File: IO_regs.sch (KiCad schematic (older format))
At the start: 77 parts, among them U17 74HC04, U4 74HC04, U42 74HC245, U43 74HC04, U44 74HC04, U45 74LS373, U46 74HC04, U47 74HC04, U48 74HC04, U49 74HC04, U50 74HC04, U51 74HC04, U52 74HC04, U6 74HC04

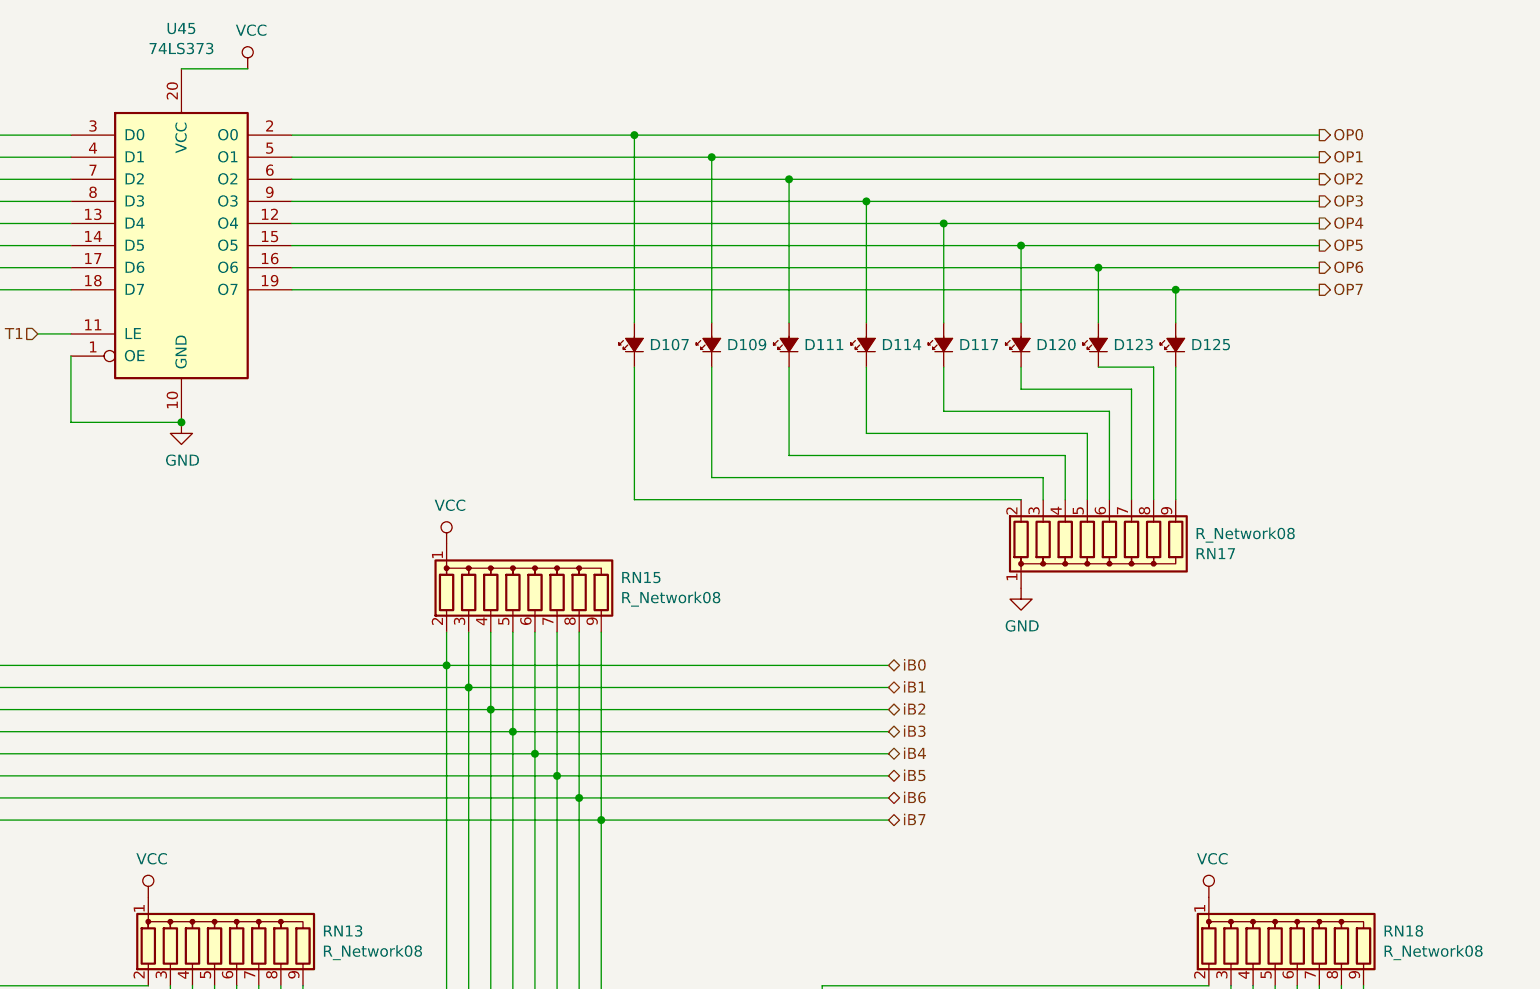
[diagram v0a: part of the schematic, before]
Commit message: start routing the OPcode register, we have a piece of the iBn bus
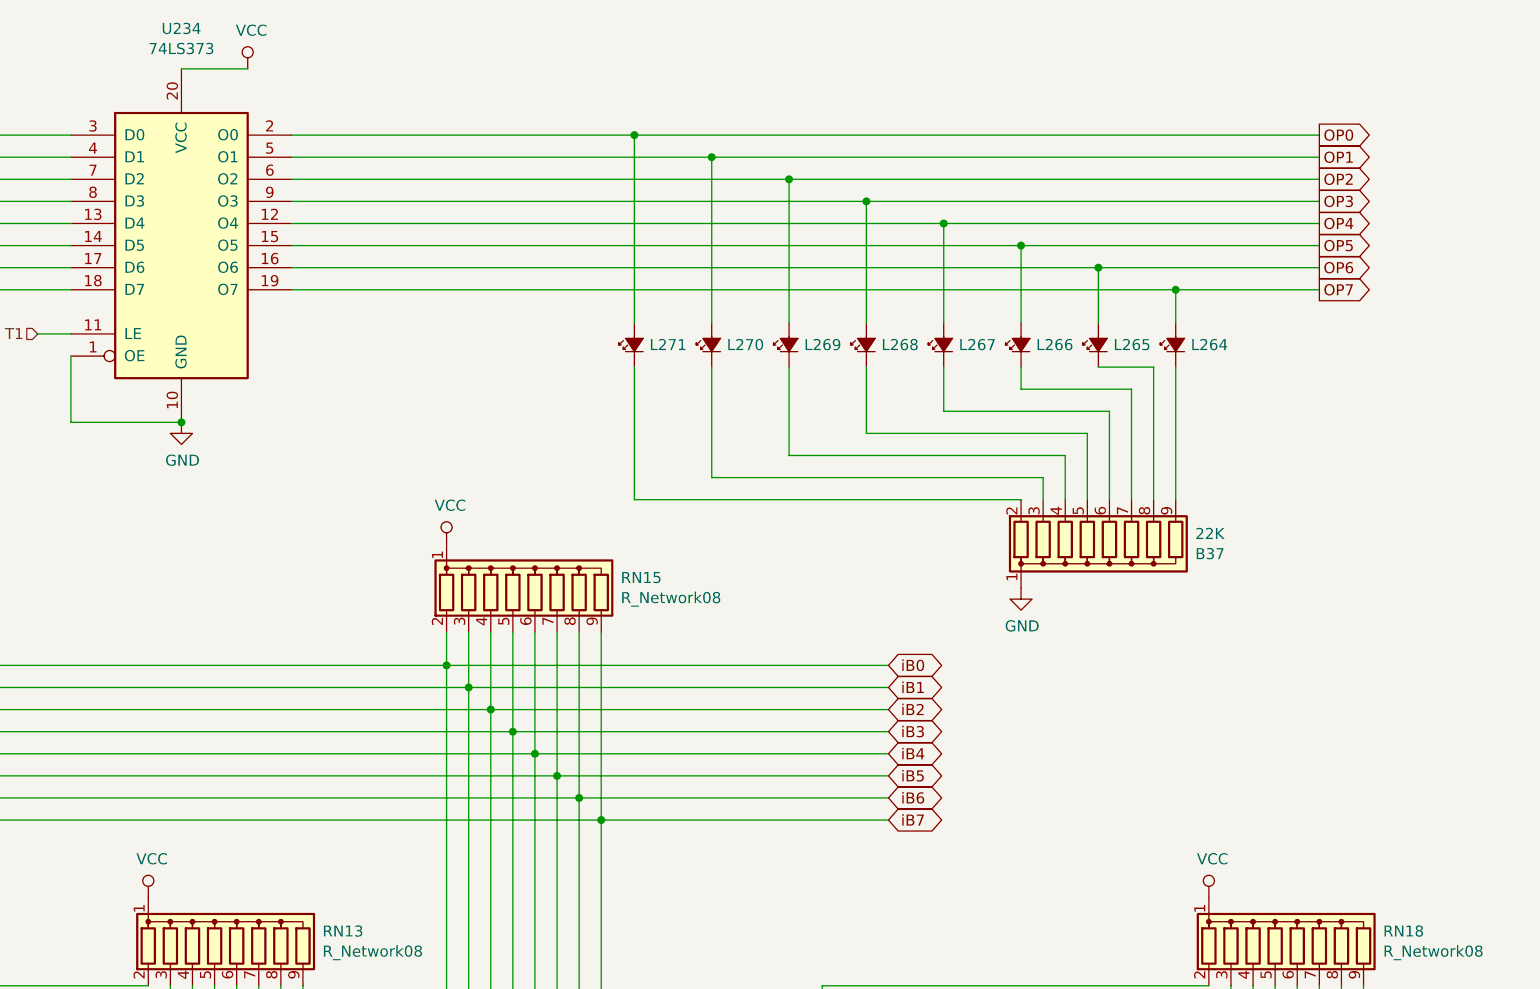
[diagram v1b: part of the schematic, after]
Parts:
- B37: renamed from RN17; value R_Network08 -> 22K
- renumbered D125 to L264, D123 to L265, D120 to L266, D117 to L267, D114 to L268, D111 to L269, D109 to L270, D107 to L271, U45 to U234
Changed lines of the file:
@@
 Wire Wire Line
 	6750 3800 6750 4650
-Text HLabel 8050 3950 2    50   BiDi ~ 0
-iB0
-Text HLabel 8050 4050 2    50   BiDi ~ 0
-iB1
-Text HLabel 8050 4150 2    50   BiDi ~ 0
-iB2
-Text HLabel 8050 4250 2    50   BiDi ~ 0
-iB3
-Text HLabel 8050 4350 2    50   BiDi ~ 0
-iB4
-Text HLabel 8050 4550 2    50   BiDi ~ 0
-iB6
-Text HLabel 8050 4650 2    50   BiDi ~ 0
-iB7
-$Comp
-L 74xx:74LS373 U45
+$Comp
+L 74xx:74LS373 U234
 U 1 1 5E589EDB
 P 4850 2050
-F 0 "U45" H 4850 3031 50  0000 C CNN
+F 0 "U234" H 4850 3031 50  0000 C CNN
 F 1 "74LS373" H 4850 2940 50  0000 C CNN
 F 2 "Package_DIP:DIP-20_W7.62mm" H 4850 2050 50  0001 C CNN
@@
 	3250 3950 6050 3950
 $Comp
-L Device:R_Network08 RN17
+L Device:R_Network08 B37
 U 1 1 5E61675D
 P 9050 3400
-F 0 "RN17" H 9438 3446 50  0000 L CNN
-F 1 "R_Network08" H 9438 3355 50  0000 L CNN
+F 0 "B37" H 9438 3446 50  0000 L CNN
+F 1 "22K" H 9438 3355 50  0000 L CNN
 F 2 "Resistor_THT:R_Array_SIP9" V 9525 3400 50  0001 C CNN
 F 3 "http://www.vishay.com/docs/31509/csc.pdf" H 9050 3400 50  0001 C CNN
@@
 $EndComp
 $Comp
-L Device:LED_Small_ALT D107
+L Device:LED_Small_ALT L271
 U 1 1 5E616763
 P 6900 2500
-F 0 "D107" V 6900 2432 50  0000 R CNN
+F 0 "L271" V 6900 2432 50  0000 R CNN
 F 1 "LED_Small_ALT" V 6855 2432 50  0001 R CNN
 F 2 "LED_THT:LED_D3.0mm" V 6900 2500 50  0001 C CNN
@@
 $EndComp
 $Comp
-L Device:LED_Small_ALT D109
+L Device:LED_Small_ALT L270
 U 1 1 5E616769
 P 7250 2500
-F 0 "D109" V 7250 2432 50  0000 R CNN
+F 0 "L270" V 7250 2432 50  0000 R CNN
 F 1 "LED_Small_ALT" V 7205 2432 50  0001 R CNN
 F 2 "LED_THT:LED_D3.0mm" V 7250 2500 50  0001 C CNN
@@
 $EndComp
 $Comp
-L Device:LED_Small_ALT D111
+L Device:LED_Small_ALT L269
 U 1 1 5E61676F
 P 7600 2500
-F 0 "D111" V 7600 2432 50  0000 R CNN
+F 0 "L269" V 7600 2432 50  0000 R CNN
 F 1 "LED_Small_ALT" V 7555 2432 50  0001 R CNN
 F 2 "LED_THT:LED_D3.0mm" V 7600 2500 50  0001 C CNN
@@
 $EndComp
 $Comp
-L Device:LED_Small_ALT D114
+L Device:LED_Small_ALT L268
 U 1 1 5E616775
 P 7950 2500
-F 0 "D114" V 7950 2432 50  0000 R CNN
+F 0 "L268" V 7950 2432 50  0000 R CNN
 F 1 "LED_Small_ALT" V 7905 2432 50  0001 R CNN
 F 2 "LED_THT:LED_D3.0mm" V 7950 2500 50  0001 C CNN
@@
 $EndComp
 $Comp
-L Device:LED_Small_ALT D117
+L Device:LED_Small_ALT L267
 U 1 1 5E61677B
 P 8300 2500
-F 0 "D117" V 8300 2432 50  0000 R CNN
+F 0 "L267" V 8300 2432 50  0000 R CNN
 F 1 "LED_Small_ALT" V 8255 2432 50  0001 R CNN
 F 2 "LED_THT:LED_D3.0mm" V 8300 2500 50  0001 C CNN
@@
 $EndComp
 $Comp
-L Device:LED_Small_ALT D120
+L Device:LED_Small_ALT L266
 U 1 1 5E616781
 P 8650 2500
-F 0 "D120" V 8650 2432 50  0000 R CNN
+F 0 "L266" V 8650 2432 50  0000 R CNN
 F 1 "LED_Small_ALT" V 8605 2432 50  0001 R CNN
 F 2 "LED_THT:LED_D3.0mm" V 8650 2500 50  0001 C CNN
@@
 $EndComp
 $Comp
-L Device:LED_Small_ALT D123
+L Device:LED_Small_ALT L265
 U 1 1 5E616787
 P 9000 2500
-F 0 "D123" V 9000 2432 50  0000 R CNN
+F 0 "L265" V 9000 2432 50  0000 R CNN
 F 1 "LED_Small_ALT" V 8955 2432 50  0001 R CNN
 F 2 "LED_THT:LED_D3.0mm" V 9000 2500 50  0001 C CNN
@@
 $EndComp
 $Comp
-L Device:LED_Small_ALT D125
+L Device:LED_Small_ALT L264
 U 1 1 5E61678D
 P 9350 2500
-F 0 "D125" V 9350 2432 50  0000 R CNN
+F 0 "L264" V 9350 2432 50  0000 R CNN
 F 1 "LED_Small_ALT" V 9305 2432 50  0001 R CNN
 F 2 "LED_THT:LED_D3.0mm" V 9350 2500 50  0001 C CNN
@@
 Wire Wire Line
 	5350 1550 6900 1550
-Text HLabel 8050 4450 2    50   BiDi ~ 0
-iB5
 Wire Wire Line
 	6900 2400 6900 1550
@@
 Wire Wire Line
 	9350 2250 10000 2250
-Text HLabel 10000 1550 2    50   Output ~ 0
-OP0
-Text HLabel 10000 1650 2    50   Output ~ 0
-OP1
-Text HLabel 10000 1750 2    50   Output ~ 0
-OP2
-Text HLabel 10000 1850 2    50   Output ~ 0
-OP3
-Text HLabel 10000 1950 2    50   Output ~ 0
-OP4
-Text HLabel 10000 2050 2    50   Output ~ 0
-OP5
-Text HLabel 10000 2150 2    50   Output ~ 0
-OP6
-Text HLabel 10000 2250 2    50   Output ~ 0
-OP7
 $Comp
 L power:VCC #PWR0134
@@
 	1    0    0    -1
 $EndComp
+Text GLabel 10000 1550 2    50   Output ~ 0
+OP0
+Text GLabel 10000 1650 2    50   Output ~ 0
+OP1
+Text GLabel 10000 1750 2    50   Output ~ 0
+OP2
+Text GLabel 10000 1850 2    50   Output ~ 0
+OP3
+Text GLabel 10000 1950 2    50   Output ~ 0
+OP4
+Text GLabel 10000 2050 2    50   Output ~ 0
+OP5
+Text GLabel 10000 2150 2    50   Output ~ 0
+OP6
+Text GLabel 10000 2250 2    50   Output ~ 0
+OP7
+Text GLabel 8050 3950 2    50   BiDi ~ 0
+iB0
+Text GLabel 8050 4050 2    50   BiDi ~ 0
+iB1
+Text GLabel 8050 4150 2    50   BiDi ~ 0
+iB2
+Text GLabel 8050 4250 2    50   BiDi ~ 0
+iB3
+Text GLabel 8050 4350 2    50   BiDi ~ 0
+iB4
+Text GLabel 8050 4450 2    50   BiDi ~ 0
+iB5
+Text GLabel 8050 4550 2    50   BiDi ~ 0
+iB6
+Text GLabel 8050 4650 2    50   BiDi ~ 0
+iB7
 $EndSCHEMATC

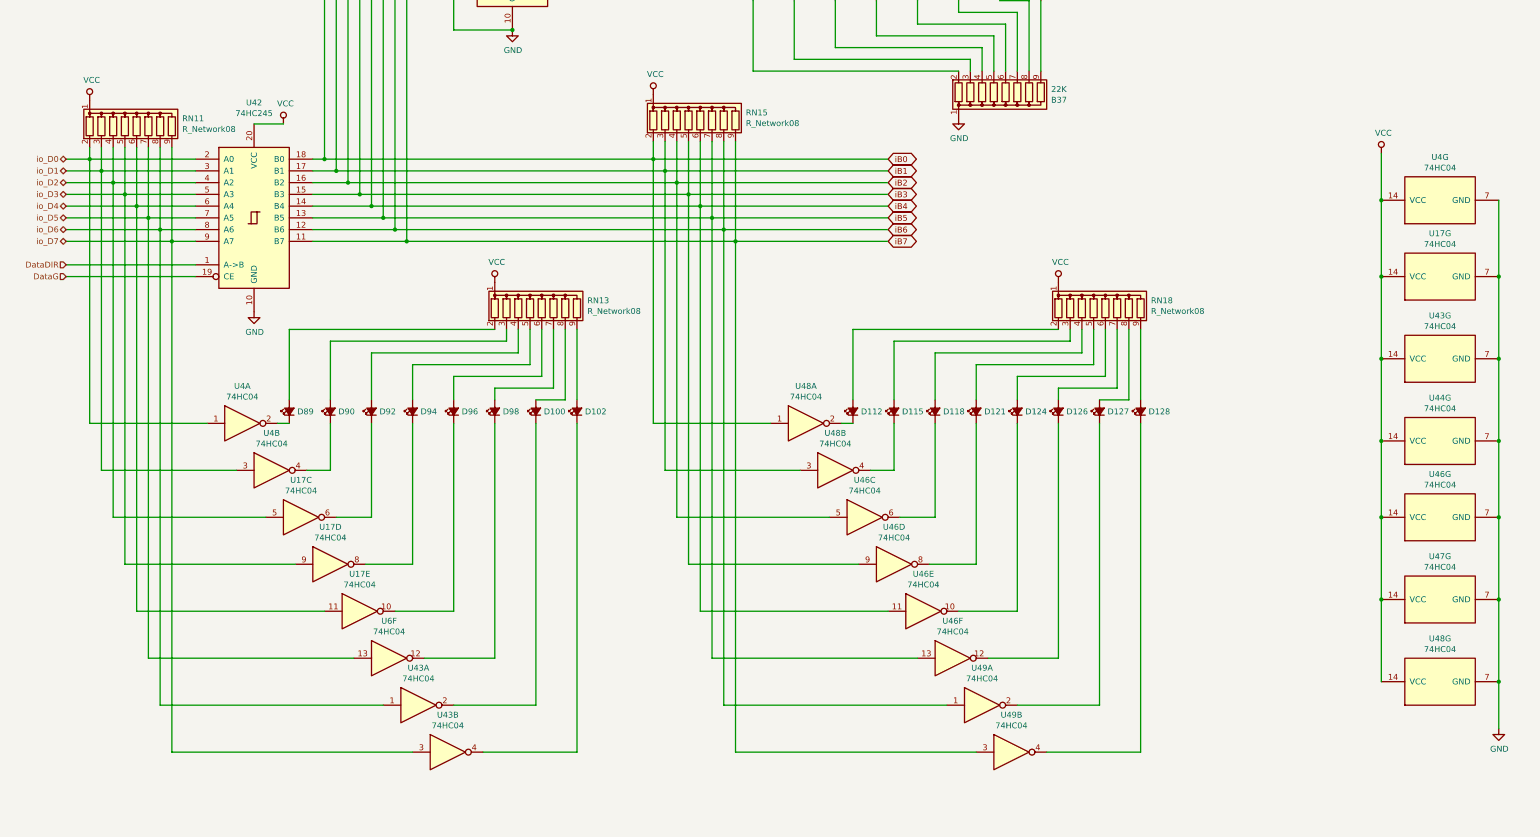
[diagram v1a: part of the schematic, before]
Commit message: place leds and inverters for the iBn bus
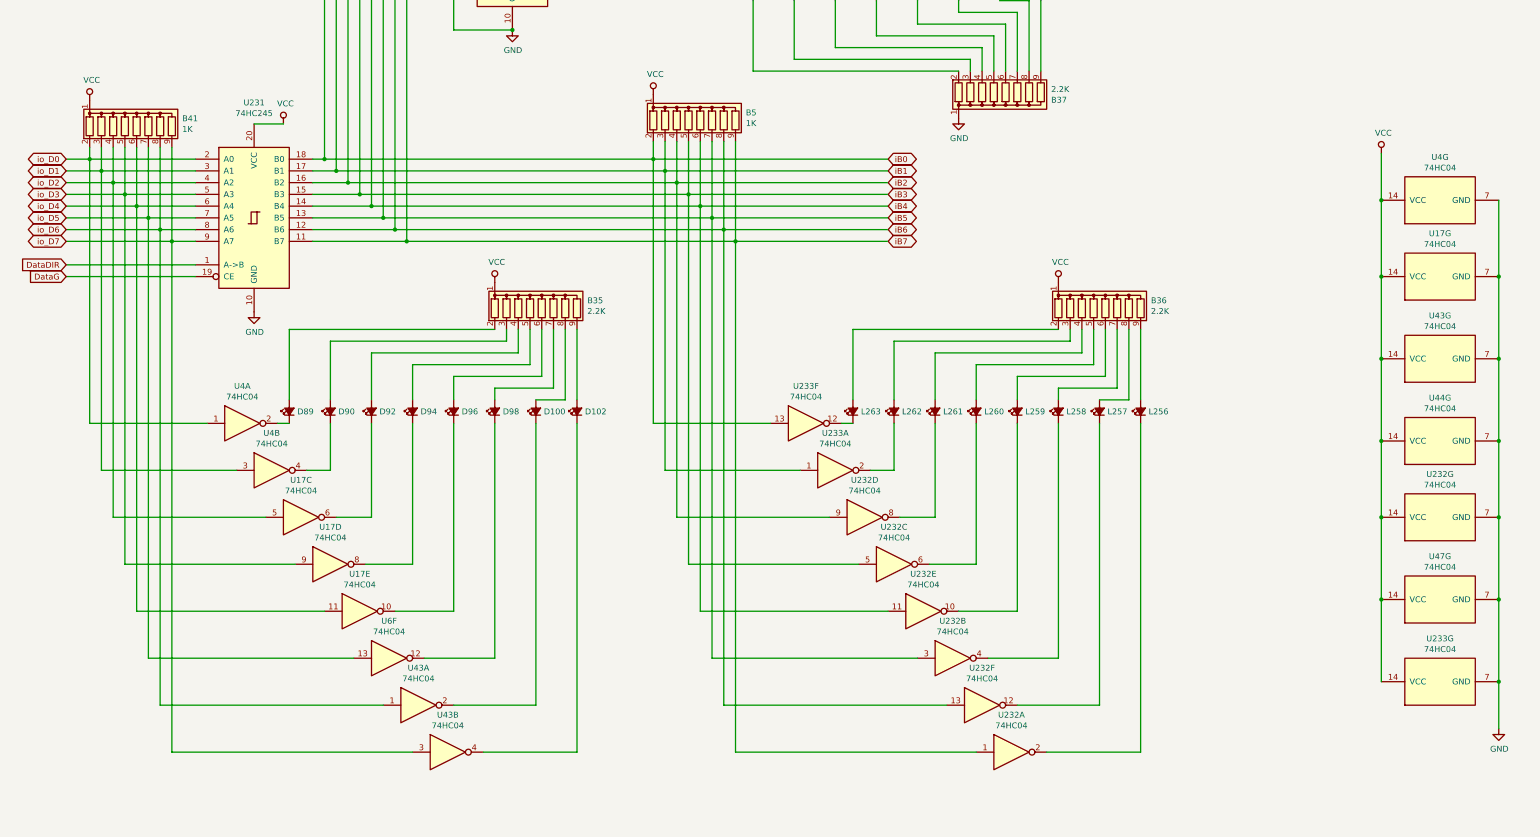
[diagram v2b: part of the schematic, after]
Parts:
- B35: renamed from RN13; value R_Network08 -> 2.2K
- B36: renamed from RN18; value R_Network08 -> 2.2K
- B37: value 22K -> 2.2K
- B41: renamed from RN11; value R_Network08 -> 1K
- B5: renamed from RN15; value R_Network08 -> 1K
- renumbered D128 to L256, D127 to L257, D126 to L258, D124 to L259, D121 to L260, D118 to L261, D115 to L262, D112 to L263, U42 to U231, U46 to U232, U49 to U232, U48 to U233
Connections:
- net iB0: now also U233.13; no longer U233.1
- net iB1: now also U233.1; no longer U233.3
- net iB2: now also U232.9; no longer U232.5
- net iB3: now also U232.5; no longer U232.9
- net iB5: now also U232.3; no longer U232.13
- net iB6: now also U232.13; no longer U232.1
- net iB7: now also U232.1; no longer U232.3
- net at L263.1 (K): now also U233.12; no longer U233.2
- net at L262.1 (K): now also U233.2; no longer U233.4
- net at L261.1 (K): now also U232.8; no longer U232.6
- net at L260.1 (K): now also U232.6; no longer U232.8
- net at L258.1 (K): now also U232.4; no longer U232.12
- net at L257.1 (K): now also U232.12; no longer U232.2
- net at L256.1 (K): now also U232.2; no longer U232.4
